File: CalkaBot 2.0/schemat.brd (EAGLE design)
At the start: 94.4 x 101.8 mm, 36 parts, among them IC1 TB6612FNG, IC2 LM339D, Q1 16MHz

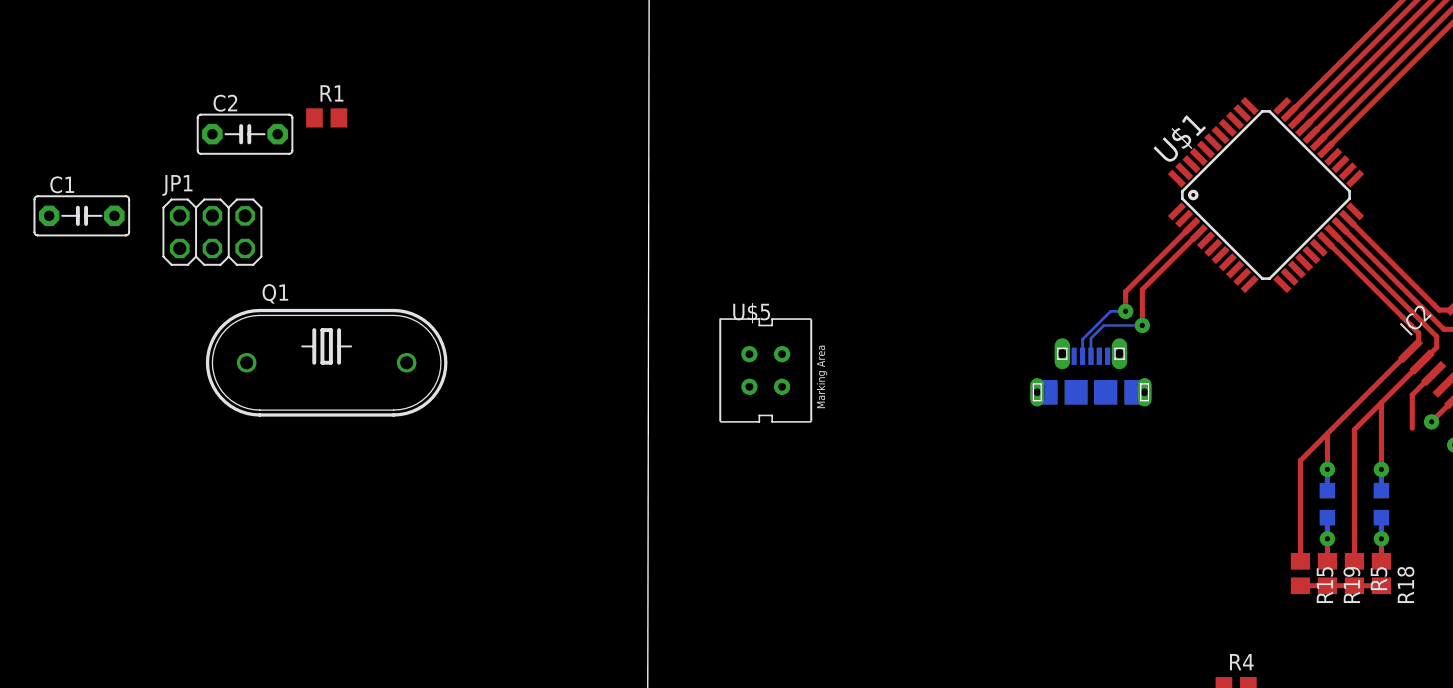
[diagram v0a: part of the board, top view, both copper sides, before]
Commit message: added resonator
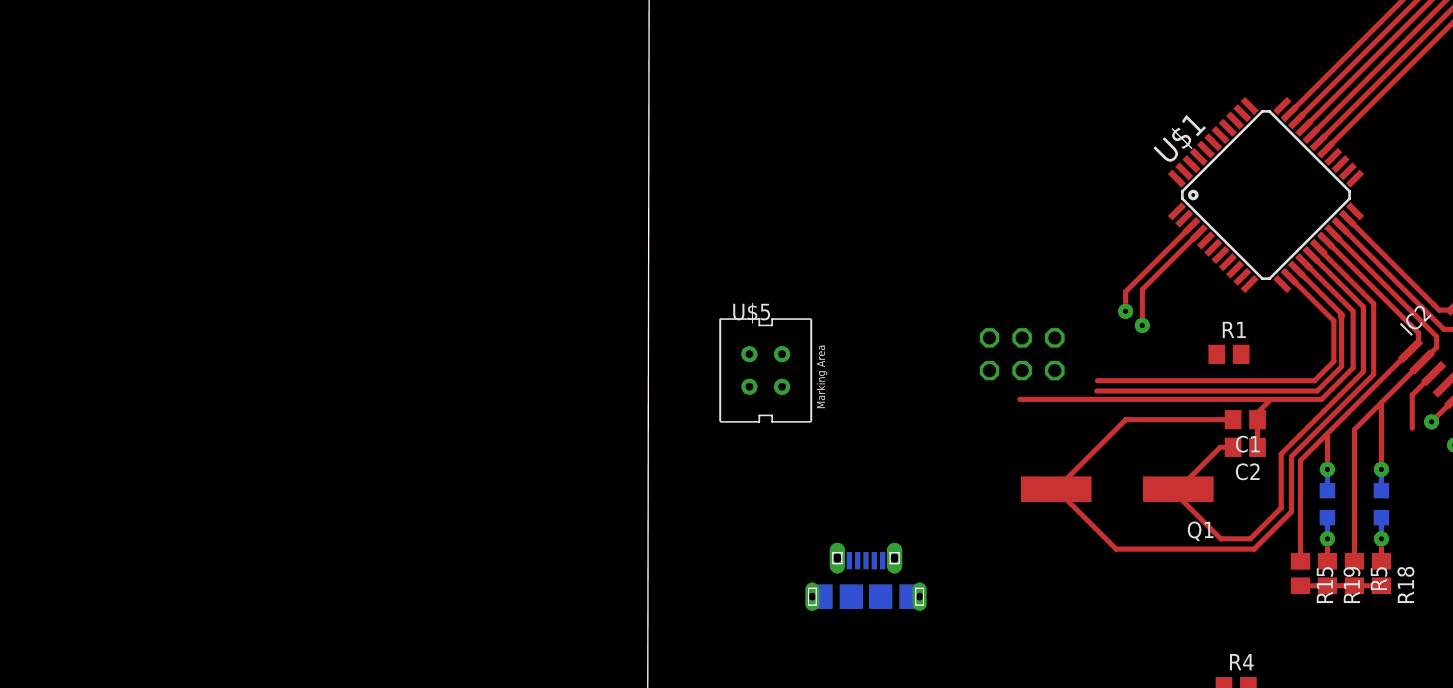
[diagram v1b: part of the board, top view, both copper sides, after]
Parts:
- C1: value 12 - 22pF -> 1.0uF; device capacitor-wima:C5B3 -> rcl:C0805
- C2: value (none) -> 1.0uF; device capacitor-wima:C5B3 -> rcl:C0805
- Q1: device crystal:HC33U-V -> crystal:CSM-7X-DU
- moved C1 91.9 mm to (48.6, 21.0), turned to 180 degrees
- moved C2 81.5 mm to (48.6, 18.8), turned to 180 degrees
- moved R1 72.6 mm to (47.3, 26.1)
- moved JP1 63.7 mm to (31.2, 26.1), flipped to the bottom, turned to 180 degrees
- moved Q1 62.3 mm to (38.6, 15.6), turned to 180 degrees
- moved U$2 23.6 mm to (19.1, 7.20)
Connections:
- net VCC: now also JP1.2
- net VCC(5): no longer JP1.2
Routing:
- net XTAL1: track 0.00 -> 62.4 mm
- net GND: track 18.0 -> 58.9 mm
- net XTAL2: track 0.00 -> 40.5 mm
- net VCC: track 17.5 -> 46.6 mm
- net RST: track 0.00 -> 27.0 mm
- net D+: track 14.8 -> 9.00 mm
- net D-: track 14.3 -> 8.77 mm

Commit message: Powiększone dziurki
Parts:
- removed R2: 100k, pot:CA6V
- added POT: 100k, pot:CA6V
- moved RESETBUTTON 84.2 mm to (18.4, 49.3)
- moved U$2 69.8 mm to (86.9, 23.7)
- moved JP1 13.8 mm to (22.9, 15.1), turned to 45 degrees
- moved R1 5.48 mm to (52.5, 27.7), turned to 90 degrees
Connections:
- net GND: now also POT.A; no longer R2.A
- net POT: now also POT.S; no longer R2.S
- net VCC: now also POT.E; no longer R2.E
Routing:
- net GND: track 58.9 -> 99.6 mm
- net SCK: track 0.00 -> 34.5 mm
- net MISO: track 0.00 -> 34.1 mm
- net MOSI: track 0.00 -> 32.2 mm
- net RST: track 27.0 -> 53.0 mm
- net D+: track 9.00 -> 0.00 mm, vias 1 -> 0
- net D-: track 8.77 -> 0.00 mm, vias 1 -> 0
- net VCC: track 46.6 -> 52.0 mm

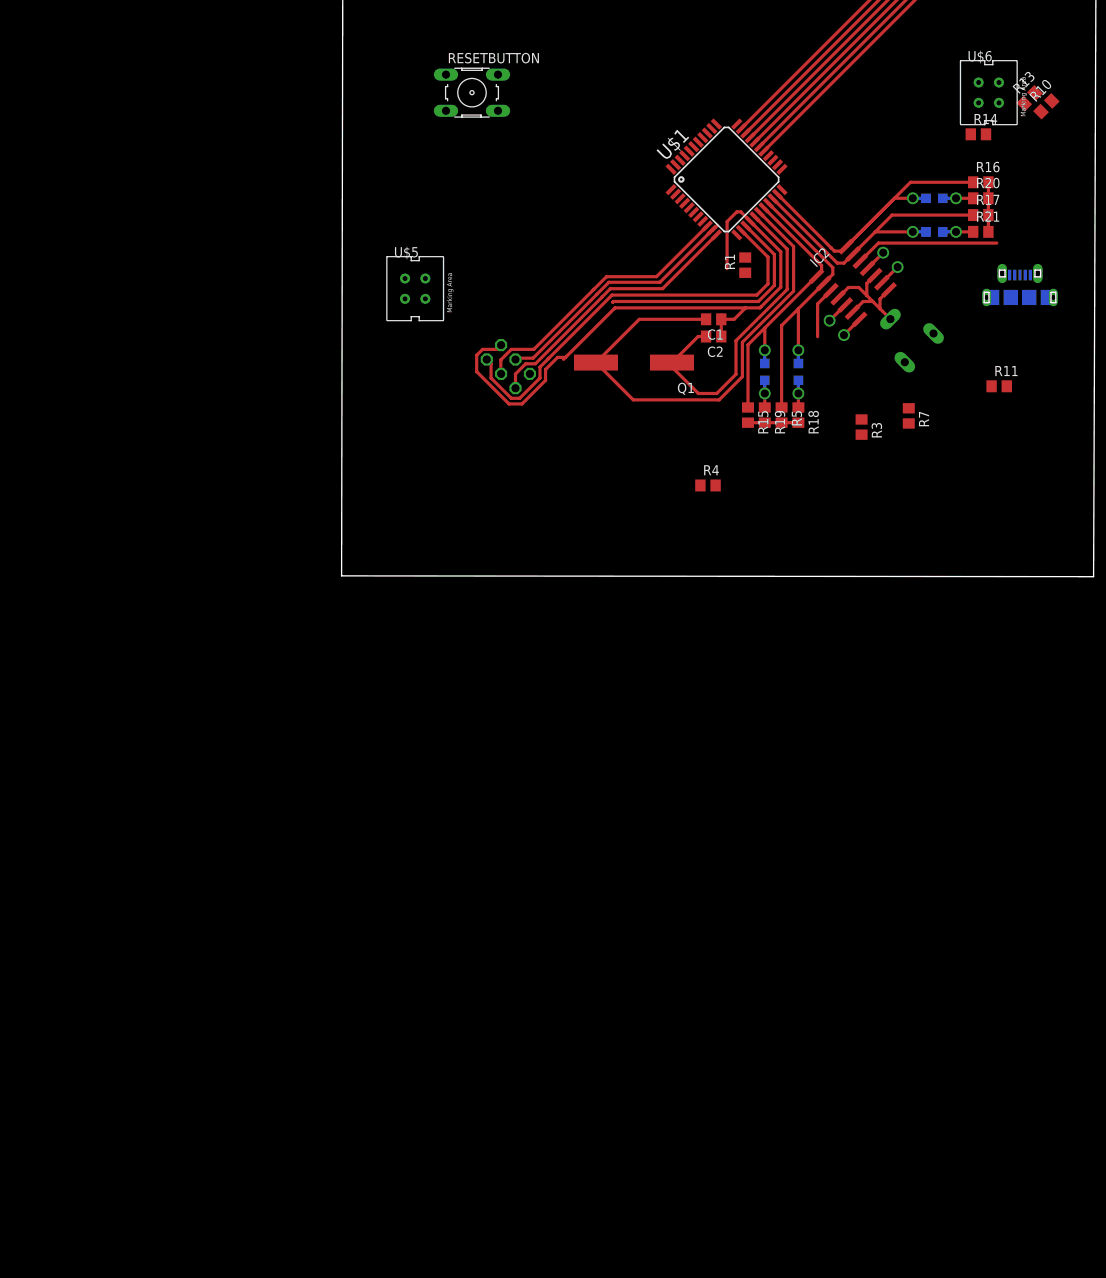
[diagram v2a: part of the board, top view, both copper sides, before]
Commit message: przyciski i usunalem isp
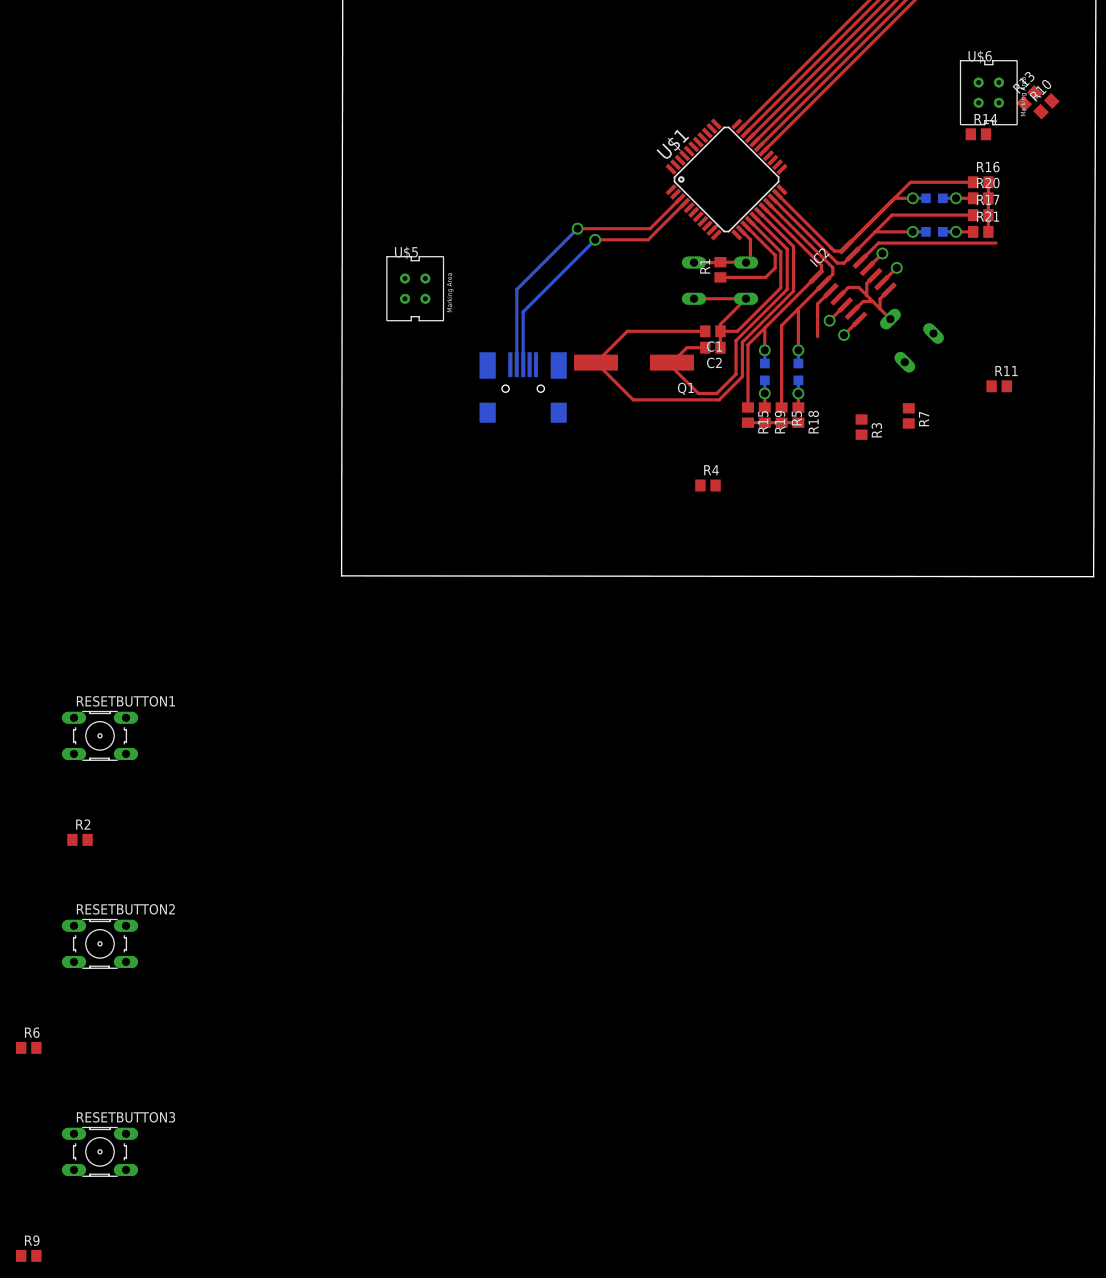
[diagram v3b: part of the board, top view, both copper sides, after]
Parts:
- removed JP1: (no value), pinhead:2X03
- removed U$2: MICRO-USB-RECEPTACLE47589-0001, con-molex-usb:47589-0001
- added R2, R6, R9: 10k, rcl:R0805
- added RESETBUTTON1, RESETBUTTON2, RESETBUTTON3: (no value), switch-omron:B3F-10XX
- added X1: MINI-USB-32005-301, con-cypressindustries:32005-301
- moved RESETBUTTON 38.9 mm to (49.4, 25.8), flipped to the bottom, turned to 180 degrees
- moved R1 3.15 mm to (49.5, 27.2)
- moved C1 1.50 mm to (48.5, 19.5)
- moved C2 1.40 mm to (48.5, 17.4)
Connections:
- removed net VCC(5): R1.1, U$2.5
- new net GND2: RESETBUTTON2.1, RESETBUTTON2.2
- new net GND3: RESETBUTTON3.1, RESETBUTTON3.2
- new net VCC2: R6.1
- new net VCC3: R9.1
- net D+: now also X1.3; no longer U$2.3
- net D-: now also X1.4; no longer U$2.4
- net GND: now also RESETBUTTON1.1, RESETBUTTON1.2, X1.1; no longer JP1.6, U$2.1
- net ID: now also X1.2; no longer U$2.2
- net MISO: now also R6.2, RESETBUTTON2.3, RESETBUTTON2.4; no longer JP1.1
- net MOSI: now also R2.2, RESETBUTTON1.3, RESETBUTTON1.4; no longer JP1.4
- net RST: no longer JP1.5
- net SCK: now also R9.2, RESETBUTTON3.3, RESETBUTTON3.4; no longer JP1.3
- net VCC: now also R1.1, R2.1, X1.5; no longer JP1.2
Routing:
- net GND: track 99.6 -> 54.6 mm
- net RST: track 53.0 -> 11.8 mm
- net D-: track 0.00 -> 34.5 mm, vias 0 -> 1
- net SCK: track 34.5 -> 0.00 mm
- net MISO: track 34.1 -> 0.00 mm
- net D+: track 0.00 -> 31.6 mm, vias 0 -> 1
- net MOSI: track 32.2 -> 0.98 mm
- net VCC: track 52.0 -> 36.1 mm
- net XTAL1: track 62.4 -> 61.7 mm
- net XTAL2: track 40.5 -> 39.9 mm

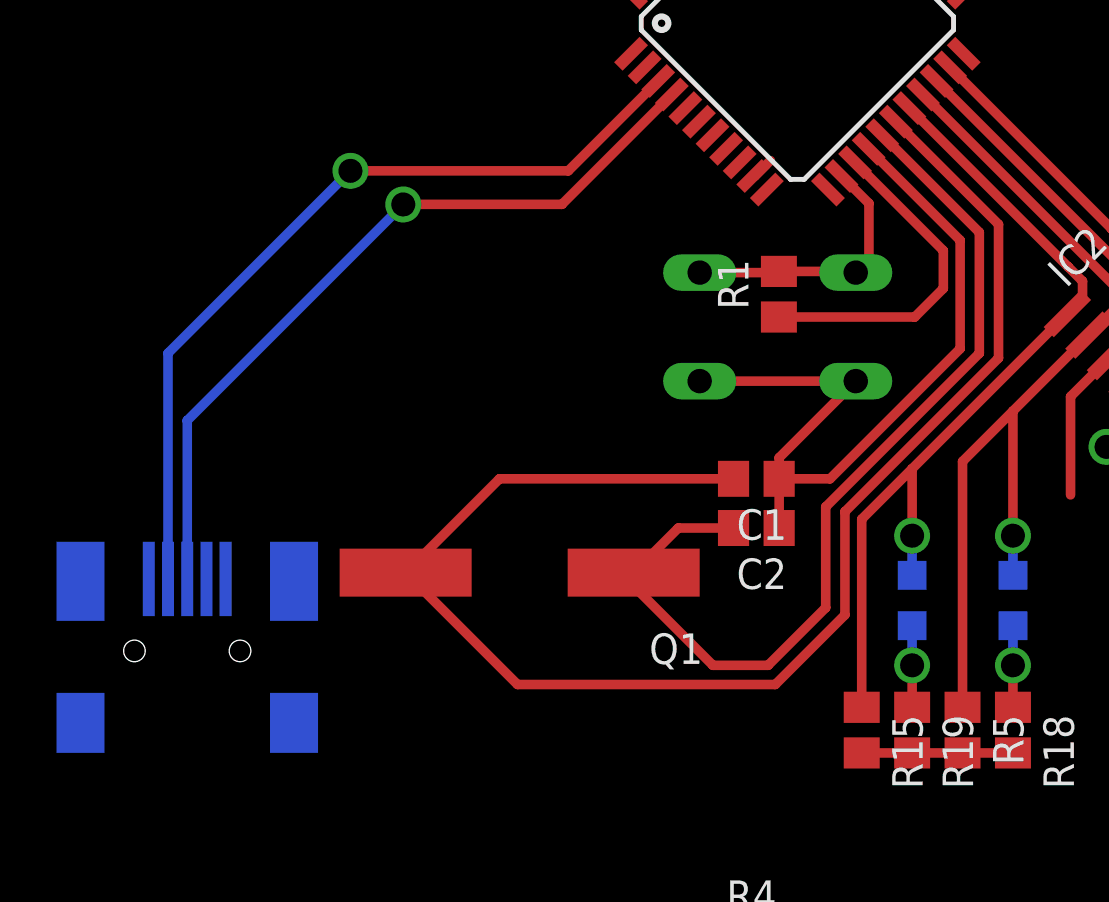
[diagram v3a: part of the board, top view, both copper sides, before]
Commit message: Dodałem stabilizator i filtrację stabilizator i przyciski
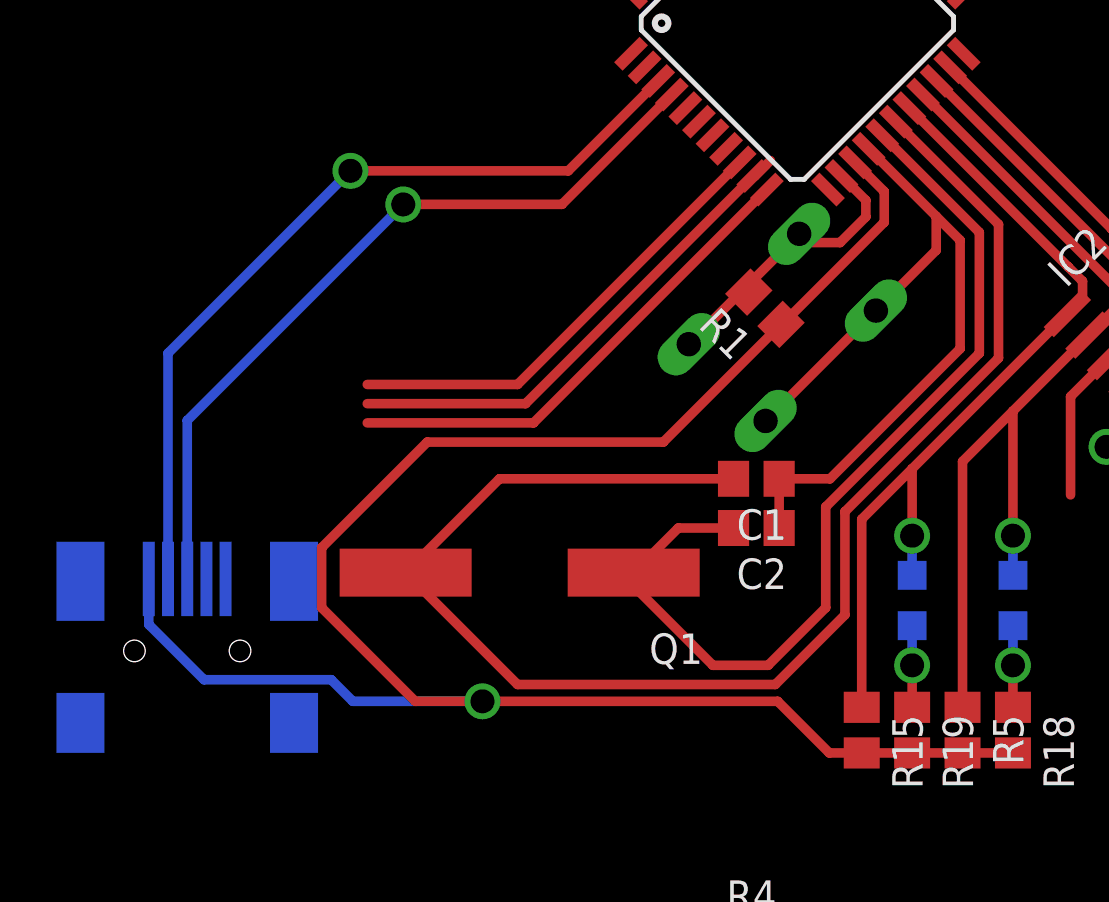
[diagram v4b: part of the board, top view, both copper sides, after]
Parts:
- moved R1 0.83 mm to (48.9, 26.6), turned to 135 degrees
- moved RESETBUTTON 0.19 mm to (49.6, 25.8), turned to 135 degrees
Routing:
- net VCC: track 36.1 -> 99.4 mm, vias 0 -> 1
- net MISO: track 0.00 -> 20.7 mm
- net MOSI: track 0.98 -> 21.0 mm
- net SCK: track 0.00 -> 19.3 mm

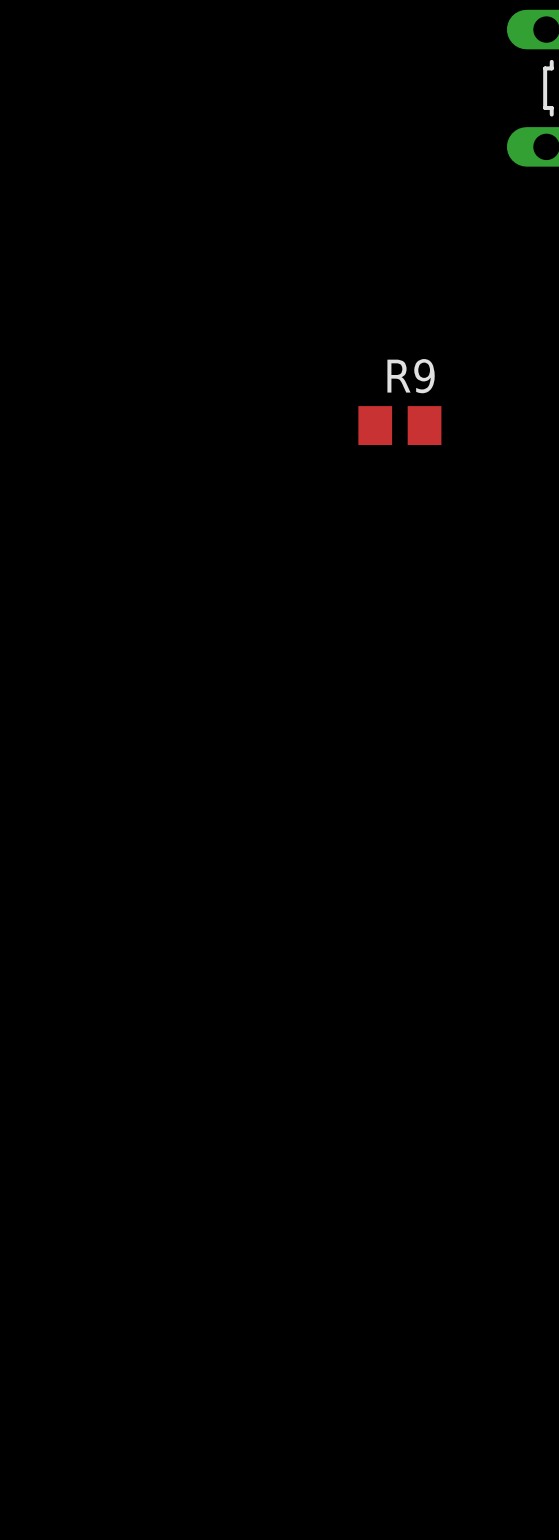
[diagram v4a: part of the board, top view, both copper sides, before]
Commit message: Dodałem filtr do zasialania silników i do sterownika
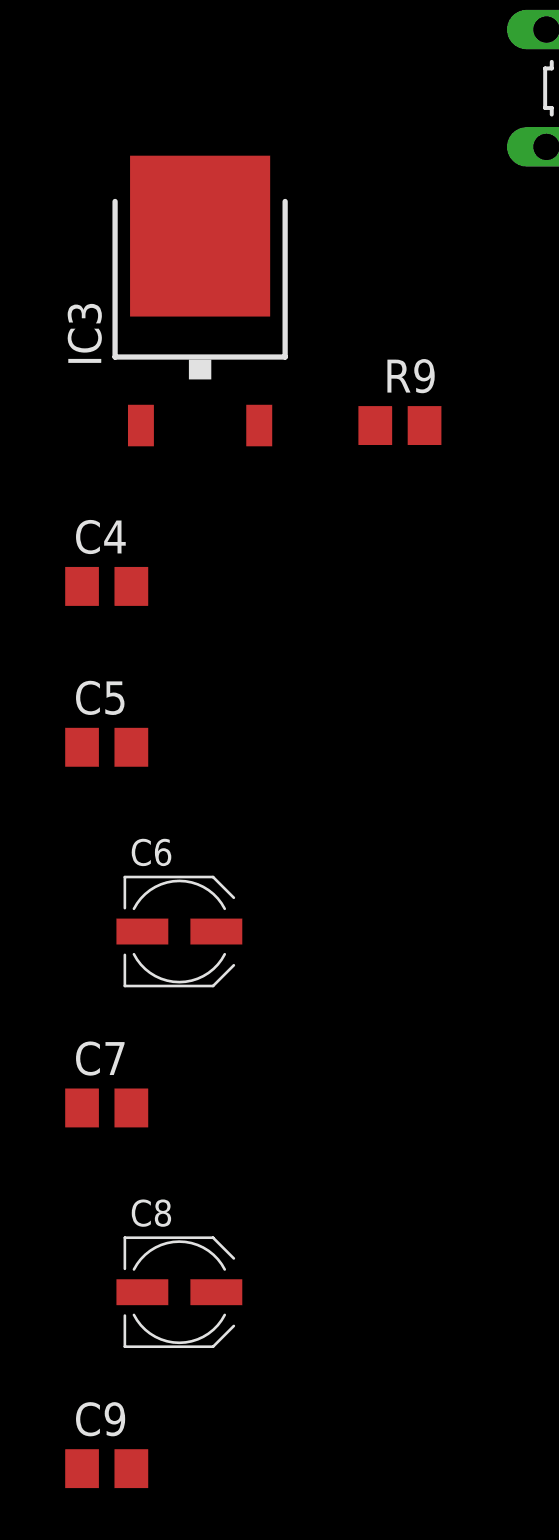
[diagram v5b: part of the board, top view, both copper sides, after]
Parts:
- added C4, C7, C9: 100nF, rcl:C0805
- added C5: 330nF, rcl:C0805
- added C6, C8: 10uF, rcl:UD-4X5,8_NICHICON
- added IC3: 7806DT, linear3:TO252
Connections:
- removed net VM1: IC1.24
- removed net VM2: IC1.13
- removed net VM3: IC1.14
- new net N$3: C4.2, IC3.2
- new net VM: C5.2, C6.+, C7.2, IC1.13, IC1.14, IC1.24, IC3.1
- net GND: now also C4.1, C5.1, C6.-, C7.1, C8.-, C9.1, IC3.3
- net VCC: now also C8.+, C9.2
